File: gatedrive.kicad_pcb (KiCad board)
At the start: 2 copper layers, 200.7 x 101.6 mm, 159 parts, among them IC1 HCPL-316J, IC10 IXDD614PI, IC11 HCPL-316J, IC12 IXDD614PI, IC13 HCPL-316J, IC14 IXDD614PI, IC15 HCPL-316J, IC16 IXDD614PI, IC2 IXDD614PI, IC3 HCPL-316J, IC4 IXDD614PI, IC5 HCPL-316J, IC6 IXDD614PI, IC7 HCPL-316J, IC8 IXDD614PI, IC9 HCPL-316J, P1 Mic General Connector, P10 CONN_01X03, P11 CONN_01X03, P12 CONN_01X03, P13 CONN_01X03, P14 CONN_01X03, P15 CONN_01X03, P16 CONN_01X03, P17 CONN_01X03, P2 CONN_01X03, P3 CONN_01X03, P4 CONN_01X03, P5 CONN_01X03, P6 CONN_01X03, P7 CONN_01X03, P8 CONN_01X03, P9 CONN_01X03

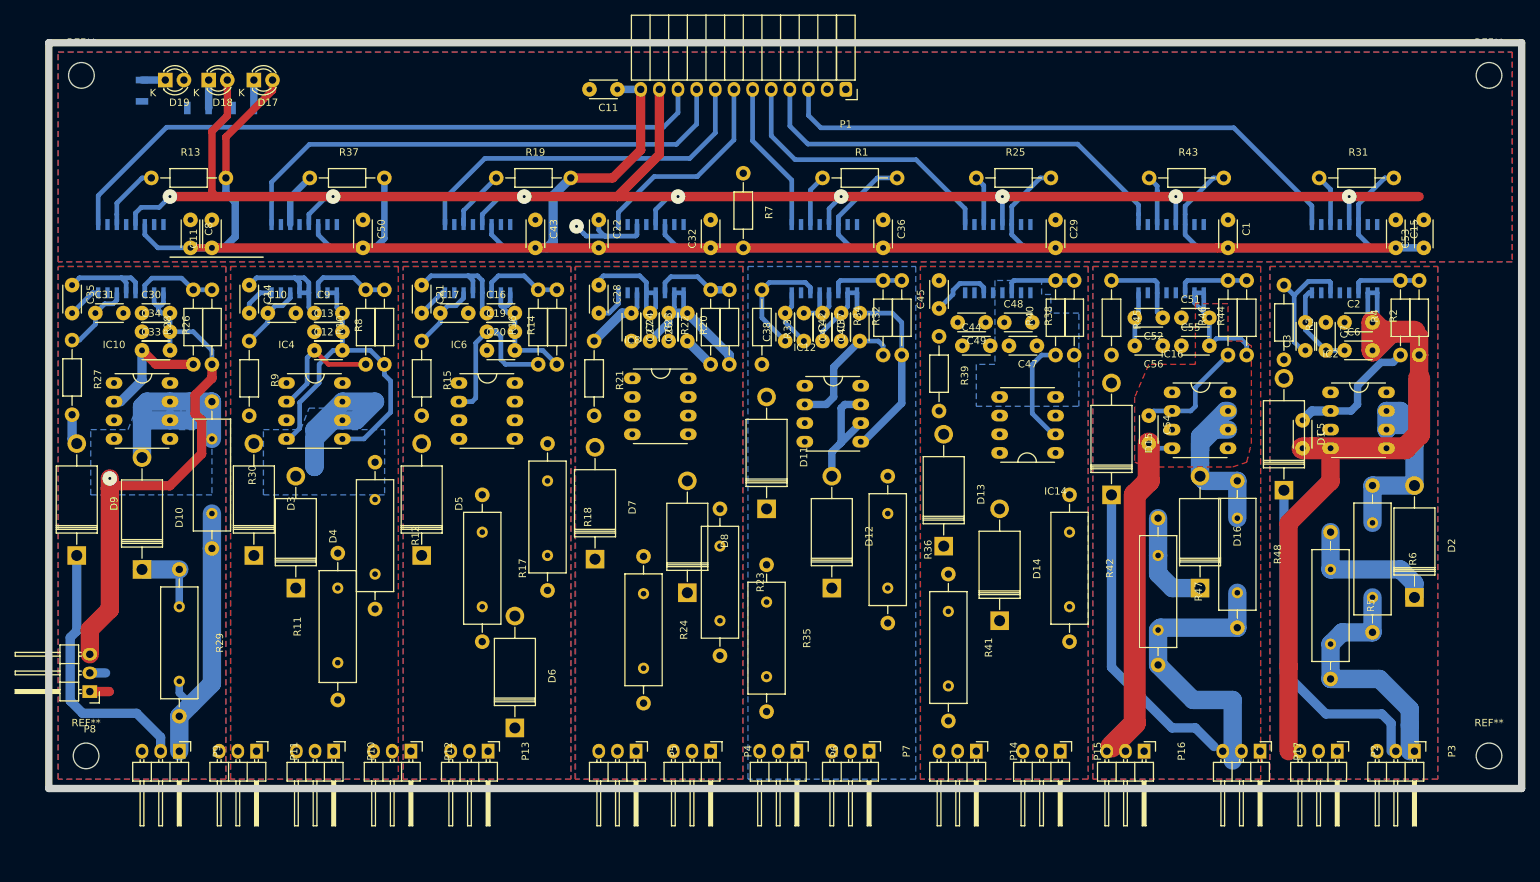
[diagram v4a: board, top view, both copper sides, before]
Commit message: cleaning the schematic
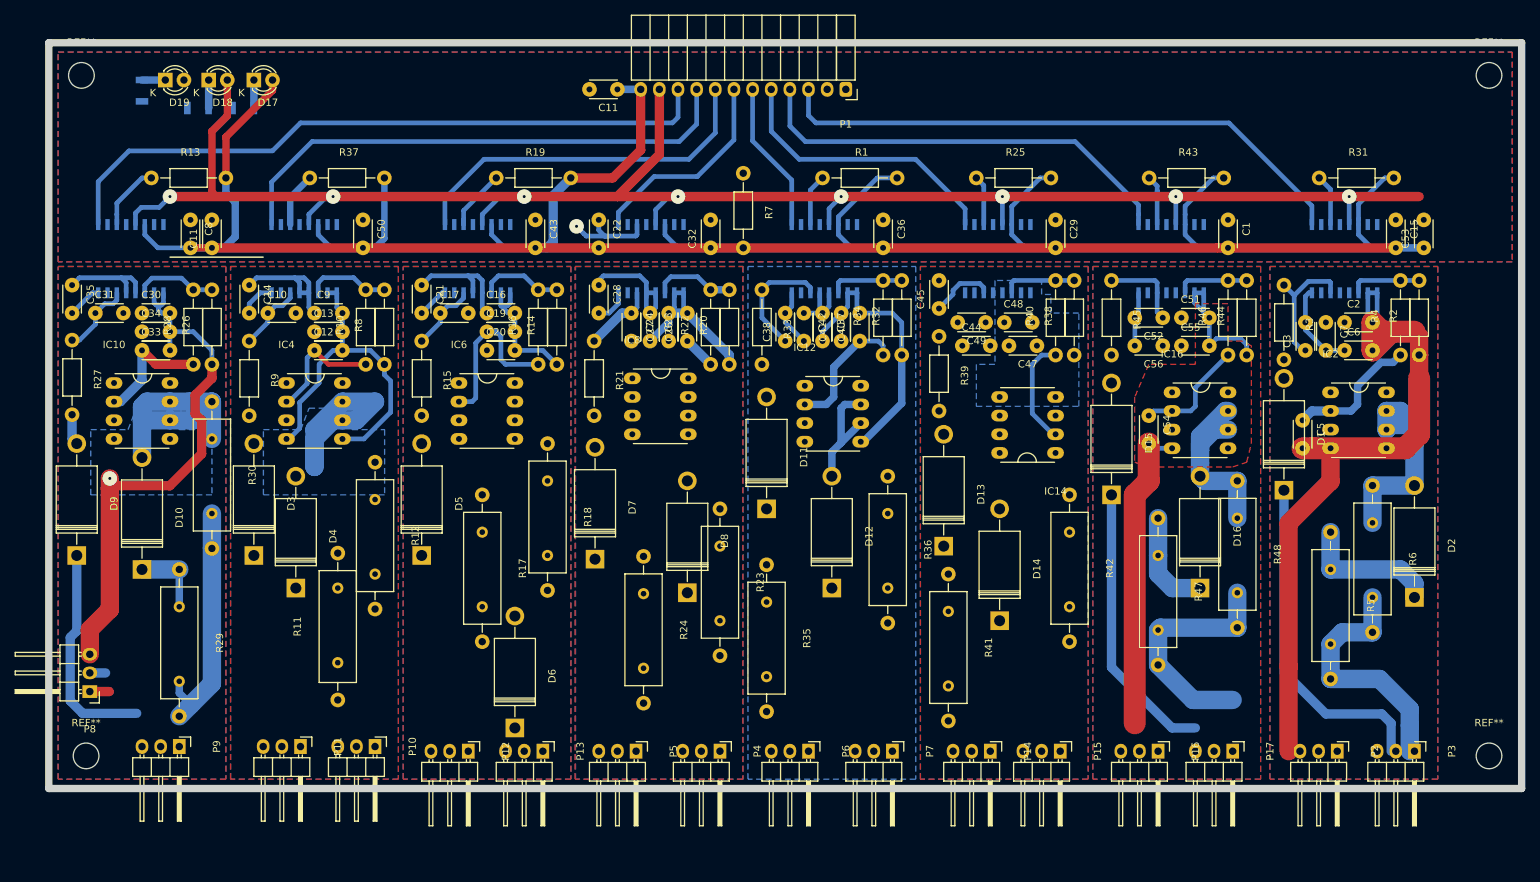
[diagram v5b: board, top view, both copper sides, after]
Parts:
- moved P12 7.82 mm to (96.2, 134.7)
- moved P13 7.46 mm to (106.3, 134.7)
- moved P11 6.03 mm to (73.3, 134.1)
- moved P10 5.67 mm to (83.5, 134.1)
- moved P17 3.73 mm to (200.3, 134.7)
- moved P7 3.17 mm to (154.0, 134.7)
- moved P14 1.91 mm to (167.3, 134.7)
- moved P16 1.91 mm to (190.2, 134.7)
- moved P6 1.59 mm to (142.5, 134.7)
- moved P4 1.27 mm to (130.5, 134.7)
- moved P9 0.63 mm to (56.8, 134.1)
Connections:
- net T1 renamed /T1
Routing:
- net G2: track 40.8 -> 32.6 mm
- net c8: track 36.5 -> 29.9 mm
- net G8: track 38.1 -> 33.3 mm
- net -5V2: track 67.1 -> 62.6 mm
- net C2: track 41.9 -> 38.3 mm
- net /T8: track 90.8 -> 92.3 mm

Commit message: completion of the layout, initial layout of the protection circuit, reducing number of circuit to 7
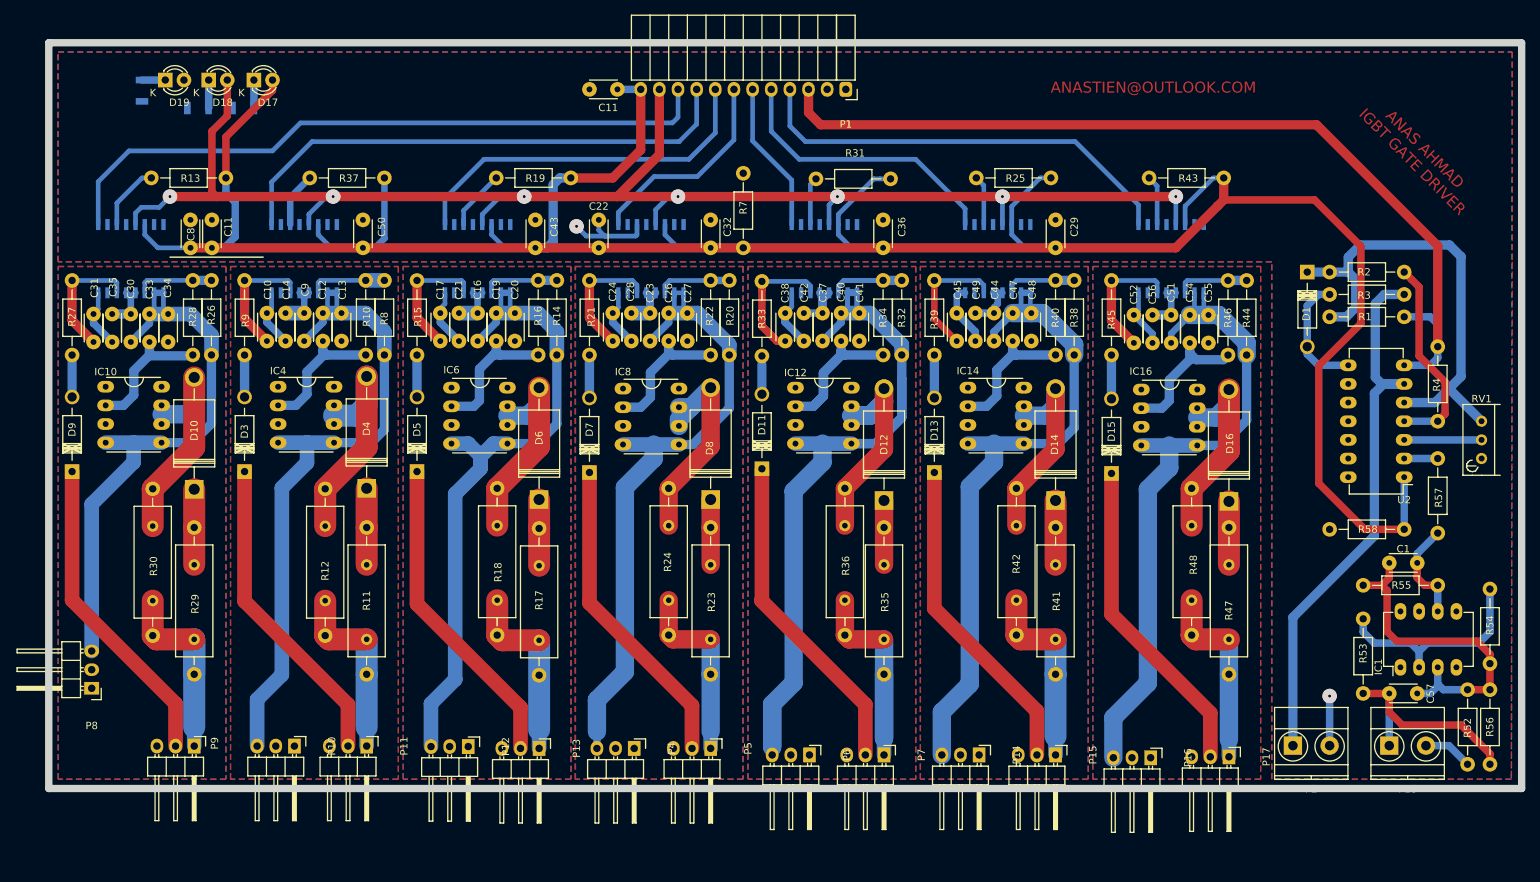
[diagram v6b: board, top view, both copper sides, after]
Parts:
- removed C15, C2, C6, C7: 0.1uF, gatedrive:C_Disc
- removed C3: 100pF, gatedrive:C_Disc
- removed C5: 10nF, gatedrive:C_Disc
- removed C53: 330pF, gatedrive:C_Disc
- removed D2: ~, Diodes_ThroughHole:Diode_DO-201AD_Horizontal_RM15
- removed IC2: IXDD614PI, gatedrive:DIP-8_W7.62mm_LongPads
- removed P3: CONN_01X03, Pin_Headers:Pin_Header_Angled_1x03
- removed R5: 60, gatedrive:Resistor_multi
- removed R6: 30ohm ,0.5W, gatedrive:Resistor_multi
- removed REF** (x4): MountingHole_3-5mm, Mounting_Holes:MountingHole_3-5mm
- added C57: 330p, gatedrive:C_Disc, F.Cu at (225.5, 126.8)
- added P18: FromShuntResistor, Terminal_Blocks:TerminalBlock_Pheonix_MKDS1.5-2pol, F.Cu at (221.7, 133.9)
- added R52: 1.24k, Resistors_ThroughHole:Resistor_Horizontal_RM10mm, F.Cu at (232.3, 126.3)
- added R53: 1.24k, Resistors_ThroughHole:Resistor_Horizontal_RM10mm, F.Cu at (218.1, 126.8)
- added R54: 20k, Resistors_ThroughHole:Resistor_Horizontal_RM10mm, F.Cu at (235.4, 112.6)
- added R55: 1.24k, Resistors_ThroughHole:Resistor_Horizontal_RM10mm, F.Cu at (218.1, 112.1)
- added R56: 1.24k, Resistors_ThroughHole:Resistor_Horizontal_RM10mm, F.Cu at (235.4, 126.3)
- added R57: 1.24k, Resistors_ThroughHole:Resistor_Horizontal_RM10mm, F.Cu at (228.3, 105.0)
- added R58: 1.24k, Resistors_ThroughHole:Resistor_Horizontal_RM10mm, F.Cu at (213.5, 104.5)
- added RV1: POT, Potentiometers:Potentiometer_Bourns_3296W_3-8Zoll_Inline_ScrewUp, F.Cu at (234.2, 94.8)
- added U2: LM393, Housings_DIP:DIP-14_W7.62mm_LongPads, F.Cu at (223.7, 97.4)
- C1: value 0.1uF -> 330p
- D1: value RGPO2-20 -> ZENER; footprint Diodes_ThroughHole:Diode_DO-201AD_Horizontal_RM15 -> Diodes_ThroughHole:Diode_DO-41_SOD81_Horizontal_RM10
- D11, D13, D15, D3, D5, D7, D9: footprint Diodes_ThroughHole:Diode_DO-201AD_Horizontal_RM15 -> Diodes_ThroughHole:Diode_DO-41_SOD81_Horizontal_RM10
- IC1: value HCPL-316J -> uA741_RevA_14Sep2012; footprint Housings_SOIC:SOIC-16_7.5x10.3mm_Pitch1.27mm -> Housings_DIP:DIP-8_W7.62mm_LongPads; moved to F.Cu
- P2: value CONN_01X03 -> FromNtc; footprint Pin_Headers:Pin_Header_Angled_1x03 -> Terminal_Blocks:TerminalBlock_Pheonix_MKDS1.5-2pol
- R1: value 10K -> 2.2MEG
- R2: value 25K -> 560
- R3: value 100 -> 10K
- R4: value 100 -> 1.24k
- moved R1 71.6 mm to (213.5, 75.5)
- moved R31 68.6 mm to (143.5, 56.7)
- moved IC1 56.2 mm to (223.2, 123.3), turned to 90 degrees
- moved C1 53.4 mm to (225.5, 109.1), turned to 180 degrees
- moved D6 31.3 mm to (105.8, 100.4)
- moved D1 29.9 mm to (210.5, 69.4), turned to 270 degrees
- moved R11 23.8 mm to (82.3, 104.2), turned to 270 degrees
- moved D14 18.1 mm to (176.2, 100.5)
- moved R35 16.8 mm to (152.8, 104.2)
- moved D4 16.7 mm to (82.3, 98.9)
- moved R3 16.4 mm to (223.7, 72.5), turned to 180 degrees
- moved R41 15.9 mm to (176.2, 104.2)
- moved IC14 14.9 mm to (164.2, 85.2), turned to 0 degrees
- moved R30 14.4 mm to (53.2, 99.0)
- moved D12 13.9 mm to (152.8, 100.5)
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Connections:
- C1 pad 1: MICSUPP -> Net-(C1-Pad1)
- C1 pad 2: ~FAULT -> Net-(C1-Pad2)
- D1 pad 1: C1 -> Net-(D1-Pad1)
- D1 pad 2: Net-(D1-Pad2) -> GND1
- IC1 pad 1: /T1 -> (no net)
- IC1 pad 2: GND1 -> Net-(IC1-Pad2)
- IC1 pad 3: MICSUPP -> Net-(C1-Pad2)
- IC1 pad 4: GND1 -> (no net)
- IC1 pad 5: ~RST -> (no net)
- IC1 pad 6: ~FAULT -> Net-(C1-Pad1)
- IC1 pad 7: Net-(IC1-Pad7) -> (no net)
- IC1 pad 8: GND1 -> (no net)
- IC11 pad 15: Net-(IC11-Pad15) -> (no net)
- IC11 pad 7: Net-(IC11-Pad7) -> (no net)
- IC13 pad 15: Net-(IC13-Pad15) -> (no net)
- IC13 pad 7: Net-(IC13-Pad7) -> (no net)
- IC15 pad 15: Net-(IC15-Pad15) -> (no net)
- IC15 pad 7: Net-(IC15-Pad7) -> (no net)
- IC3 pad 15: Net-(IC3-Pad15) -> (no net)
- IC3 pad 7: Net-(IC3-Pad7) -> (no net)
- IC5 pad 15: Net-(IC5-Pad15) -> (no net)
- IC5 pad 7: Net-(IC5-Pad7) -> (no net)
- IC7 pad 15: Net-(IC7-Pad15) -> (no net)
- IC7 pad 7: Net-(IC7-Pad7) -> (no net)
- IC9 pad 15: Net-(IC9-Pad15) -> (no net)
- IC9 pad 7: Net-(IC9-Pad7) -> (no net)
- P1 pad 3: /T1 -> ~OVERTEMP
- P11 pad 1: COM7 -> G7
- P11 pad 3: G7 -> COM7
- P13 pad 1: COM6 -> G6
- P13 pad 3: G6 -> COM6
- P2 pad 1: COM1 -> Net-(P2-Pad1)
- P2 pad 2: 15v1 -> MICSUPP
- R1 pad 1: MICSUPP -> Net-(D1-Pad1)
- R1 pad 2: ~FAULT -> ~OVERTEMP
- R2 pad 1: -5V1 -> MICSUPP
- R2 pad 2: Net-(IC1-Pad11) -> Net-(D1-Pad1)
- R3 pad 1: Net-(C3-Pad1) -> Net-(P2-Pad1)
- R3 pad 2: Net-(D1-Pad2) -> GND1
- R4 pad 1: Net-(C5-Pad1) -> MICSUPP
- R4 pad 2: Net-(IC1-Pad11) -> ~OVERTEMP
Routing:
- net ~OVERTEMP: track 0.00 -> 124.7 mm
- net -5V1: track 109.5 -> 0.00 mm
- net -5V3: track 0.00 -> 94.4 mm
- net -5V4: track 37.2 -> 123.9 mm
- net /T1: track 79.8 -> 0.00 mm
- net -5V6: track 18.5 -> 94.9 mm
- net Net-(P2-Pad1): track 0.00 -> 75.7 mm
- net -5V5: track 24.5 -> 92.5 mm
- net Net-(D1-Pad1): track 0.00 -> 65.6 mm
- net -5V7: track 47.1 -> 94.3 mm
- net C1: track 46.1 -> 0.00 mm
- net Net-(C1-Pad2): track 0.00 -> 45.9 mm
- net C4: track 0.00 -> 44.9 mm
- net C3: track 0.00 -> 44.3 mm
- net C6: track 0.00 -> 43.6 mm
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- added copper zone on F.Cu, net COM4
- removed copper zone on F.Cu, net -5V2
- removed copper zone on B.Cu, net -5V3
- removed copper zone on B.Cu, net -5V7
- removed copper zone on B.Cu, net -5v8
- removed copper zone on B.Cu, net 15v1
- removed copper zone on F.Cu, net COM1
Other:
- outline, holes or cut-outs redrawn
- board text added: "ANAS AHMAD IGBT GATE DRIVER"
- board text added: "ANASTIEN@OUTLOOK.COM"

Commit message: yet another enhancements .
the protection section still is incomplete.
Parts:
- added REF**: MountingHole_2.5mm, Mounting_Holes:MountingHole_2.5mm, F.Cu at (125.7, 134.0)
- added REF**: MountingHole_2.5mm, Mounting_Holes:MountingHole_2.5mm, F.Cu at (196.2, 134.0)
- added REF**: MountingHole_2.5mm, Mounting_Holes:MountingHole_2.5mm, F.Cu at (230.5, 47.6)
- added REF**: MountingHole_2.5mm, Mounting_Holes:MountingHole_2.5mm, F.Cu at (166.4, 48.9)
- added REF**: MountingHole_2.5mm, Mounting_Holes:MountingHole_2.5mm, F.Cu at (95.9, 48.9)
- added REF**: MountingHole_2.5mm, Mounting_Holes:MountingHole_2.5mm, F.Cu at (232.4, 134.0)
- added REF**: MountingHole_2.5mm, Mounting_Holes:MountingHole_2.5mm, F.Cu at (56.5, 134.0)
- moved R58 66.1 mm to (175.9, 50.2)
- moved U2 52.3 mm to (191.8, 55.9), turned to 90 degrees
- moved P2 51.7 mm to (223.5, 84.5), turned to 90 degrees
- moved R57 47.8 mm to (221.0, 57.8)
- moved RV1 35.5 mm to (226.1, 60.3), turned to 180 degrees
- moved R4 29.1 mm to (211.5, 66.0)
- moved D11 27.4 mm to (151.8, 118.7)
- moved D3 27.1 mm to (81.3, 118.7)
- moved D5 27.1 mm to (104.8, 118.7)
- moved D9 27.1 mm to (57.8, 118.7)
- moved D13 27.0 mm to (175.3, 118.7)
- moved D7 27.0 mm to (128.3, 118.7)
- moved D15 26.5 mm to (198.8, 118.7)
- moved R53 23.2 mm to (232.4, 108.6)
- moved C1 19.5 mm to (226.1, 89.5)
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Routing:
- net ~FAULT: track 380.7 -> 317.9 mm
- net Net-(C1-Pad1): track 14.0 -> 70.6 mm
- net ~OVERTEMP: track 124.7 -> 74.0 mm
- net MICSUPP: track 93.1 -> 53.7 mm, vias 2 -> 0
- net Net-(RV1-Pad2): track 10.5 -> 39.4 mm
- net Net-(R57-Pad2): track 4.57 -> 31.4 mm
- net Net-(P2-Pad1): track 75.7 -> 50.6 mm
- net Net-(D11-Pad2): track 4.06 -> 27.1 mm
- net -5V4: track 123.9 -> 101.6 mm
- net Net-(D5-Pad2): track 5.71 -> 27.8 mm
- net Net-(D7-Pad2): track 5.84 -> 27.8 mm
- net Net-(D3-Pad2): track 5.71 -> 27.5 mm
- net Net-(D9-Pad2): track 5.71 -> 27.5 mm
- net Net-(D13-Pad2): track 5.84 -> 27.5 mm
- net Net-(D15-Pad2): track 5.97 -> 27.5 mm
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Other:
- board outline removed
- board text removed: "ANAS AHMAD IGBT GATE DRIVER"
- board text removed: "ANASTIEN@OUTLOOK.COM"

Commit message: packup
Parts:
- removed the C1 at (226.1, 89.5)
- removed C10, C17, C24, C31, C38, C45, C52: 100pF, gatedrive:C_Disc
- removed C11 (x2), C32: 330pF, gatedrive:C_Disc
- removed C12, C19, C26, C33, C40, C47, C54: 10nF, gatedrive:C_Disc
- removed C13, C14, C16, C20, C21, C22, C23, C27, C28, C29, C30, C34, C35, C36, C37, C41, C42, C43, C44, C48, C49, C50, C51, C55, C56, C8, C9: 0.1uF, gatedrive:C_Disc
- removed C57: 330p, gatedrive:C_Disc
- removed D1: ZENER, Diodes_ThroughHole:Diode_DO-41_SOD81_Horizontal_RM10
- removed D10, D12, D14, D16, D4, D6, D8: ~, Diodes_ThroughHole:Diode_DO-201AD_Horizontal_RM15
- removed D11, D13, D15, D3, D5, D7, D9: RGPO2-20, Diodes_ThroughHole:Diode_DO-41_SOD81_Horizontal_RM10
- removed D17, D18, D19: LED, LEDs:LED-3MM
- removed IC1: uA741_RevA_14Sep2012, Housings_DIP:DIP-8_W7.62mm_LongPads
- removed IC10, IC12, IC14, IC16, IC4, IC6, IC8: IXDD614PI, gatedrive:DIP-8_W7.62mm_LongPads
- removed IC11, IC13, IC15, IC3, IC5, IC7, IC9: HCPL-316J, Housings_SOIC:SOIC-16_7.5x10.3mm_Pitch1.27mm
- removed P1: Mic General Connector, Socket_Strips:Socket_Strip_Angled_1x12
- removed P10, P11, P12, P13, P14, P15, P16, P17, P4, P5, P6, P7, P8, P9: CONN_01X03, Pin_Headers:Pin_Header_Angled_1x03
- removed P18: FromShuntResistor, Terminal_Blocks:TerminalBlock_Pheonix_MKDS1.5-2pol
- removed P2: FromNtc, Terminal_Blocks:TerminalBlock_Pheonix_MKDS1.5-2pol
- removed R1: 2.2MEG, Resistors_ThroughHole:Resistor_Horizontal_RM10mm
- removed R10, R15, R16, R21, R22, R27, R28, R33, R34, R39, R40, R45, R46, R9: 100, Resistors_ThroughHole:Resistor_Horizontal_RM10mm
- removed R11, R17, R23, R29, R35, R41, R47: 60, gatedrive:Resistor_multi
- removed R12, R18, R24, R30, R36, R42, R48: 30ohm ,0.5W, gatedrive:Resistor_multi
- removed R13, R19, R25, R3, R31, R37, R43, R7: 10K, Resistors_ThroughHole:Resistor_Horizontal_RM10mm
- removed R14, R20, R26, R32, R38, R44, R8: 25K, Resistors_ThroughHole:Resistor_Horizontal_RM10mm
- removed R2: 560, Resistors_ThroughHole:Resistor_Horizontal_RM10mm
- removed R4, R52, R53, R55, R56, R57, R58: 1.24k, Resistors_ThroughHole:Resistor_Horizontal_RM10mm
- removed R49, R50, R51: R, Resistors_SMD:R_1206
- removed R54: 20k, Resistors_ThroughHole:Resistor_Horizontal_RM10mm
- removed REF** (x7): MountingHole_2.5mm, Mounting_Holes:MountingHole_2.5mm
- removed RV1: POT, Potentiometers:Potentiometer_Bourns_3296W_3-8Zoll_Inline_ScrewUp
- removed U2: LM393, Housings_DIP:DIP-14_W7.62mm_LongPads
- added C1: 0.1u, gatedrive:C_Disc, F.Cu at (231.8, 99.7)
- added C1: 0.1u, gatedrive:C_Disc, F.Cu at (232.4, 64.8)
- added C201: 0.1uF, gatedrive:C_Disc, F.Cu at (201.3, 58.4)
- added C202: 330pF, gatedrive:C_Disc, F.Cu at (208.3, 70.5)
- added C203: 0.1uF, gatedrive:C_Disc, F.Cu at (205.1, 80.0)
- added C204: 0.1uF, gatedrive:C_Disc, F.Cu at (197.5, 83.8)
- added C205: 0.1uF, gatedrive:C_Disc, F.Cu at (200.0, 80.0)
- added C206: 100pF, gatedrive:C_Disc, F.Cu at (194.9, 83.8)
- added C207: 10nF, gatedrive:C_Disc, F.Cu at (202.6, 83.8)
- added C301: 0.1uF, gatedrive:C_Disc, F.Cu at (177.2, 57.8)
- added C302: 330pF, gatedrive:C_Disc, F.Cu at (184.8, 71.1)
- added C303: 0.1uF, gatedrive:C_Disc, F.Cu at (181.6, 80.0)
- added C304: 0.1uF, gatedrive:C_Disc, F.Cu at (174.0, 83.8)
- added C305: 0.1uF, gatedrive:C_Disc, F.Cu at (176.5, 80.0)
- added C306: 100pF, gatedrive:C_Disc, F.Cu at (171.4, 83.8)
- added C307: 10nF, gatedrive:C_Disc, F.Cu at (179.1, 83.8)
- added C401: 0.1uF, gatedrive:C_Disc, F.Cu at (154.9, 57.8)
- added C402: 330pF, gatedrive:C_Disc, F.Cu at (161.3, 71.1)
- added C403: 0.1uF, gatedrive:C_Disc, F.Cu at (158.1, 80.0)
- added C404: 0.1uF, gatedrive:C_Disc, F.Cu at (150.5, 83.8)
- added C405: 0.1uF, gatedrive:C_Disc, F.Cu at (153.0, 80.0)
- added C406: 100pF, gatedrive:C_Disc, F.Cu at (148.0, 83.8)
- added C407: 10nF, gatedrive:C_Disc, F.Cu at (155.6, 83.8)
- added C501: 0.1uF, gatedrive:C_Disc, F.Cu at (122.6, 67.3)
- added C502: 330pF, gatedrive:C_Disc, F.Cu at (137.8, 71.1)
- added C503: 0.1uF, gatedrive:C_Disc, F.Cu at (134.6, 80.0)
- added C504: 0.1uF, gatedrive:C_Disc, F.Cu at (127.0, 83.8)
- added C505: 0.1uF, gatedrive:C_Disc, F.Cu at (129.5, 80.0)
- added C506: 100pF, gatedrive:C_Disc, F.Cu at (124.5, 83.8)
- added C507: 10nF, gatedrive:C_Disc, F.Cu at (132.1, 83.8)
- added C601: 0.1uF, gatedrive:C_Disc, F.Cu at (111.1, 57.8)
- added C602: 330pF, gatedrive:C_Disc, F.Cu at (125.1, 49.5)
- added C602: 330pF, gatedrive:C_Disc, F.Cu at (116.2, 71.1)
- added C603: 0.1uF, gatedrive:C_Disc, F.Cu at (111.1, 80.0)
- added C604: 0.1uF, gatedrive:C_Disc, F.Cu at (103.5, 83.8)
- added C605: 0.1uF, gatedrive:C_Disc, F.Cu at (106.0, 80.0)
- added C606: 100pF, gatedrive:C_Disc, F.Cu at (101.0, 83.8)
- added C607: 10nF, gatedrive:C_Disc, F.Cu at (108.6, 83.8)
- added C701: 0.1uF, gatedrive:C_Disc, F.Cu at (86.4, 57.8)
- added C702: 330pF, gatedrive:C_Disc, F.Cu at (90.8, 71.1)
- added C703: 0.1uF, gatedrive:C_Disc, F.Cu at (87.6, 80.0)
- added C704: 0.1uF, gatedrive:C_Disc, F.Cu at (80.0, 83.8)
- added C705: 0.1uF, gatedrive:C_Disc, F.Cu at (82.5, 80.0)
- added C706: 100pF, gatedrive:C_Disc, F.Cu at (77.5, 83.8)
- added C707: 10nF, gatedrive:C_Disc, F.Cu at (85.1, 83.8)
- added C801: 33pf, gatedrive:C_Disc, F.Cu at (219.1, 123.8)
- added C802: 33p, gatedrive:C_Disc, F.Cu at (226.1, 106.0)
- added C901: 0.1uF, gatedrive:C_Disc, F.Cu at (64.8, 57.8)
- added C902: 330pF, gatedrive:C_Disc, F.Cu at (68.6, 71.1)
- added C903: 0.1uF, gatedrive:C_Disc, F.Cu at (64.1, 80.0)
- added C904: 0.1uF, gatedrive:C_Disc, F.Cu at (56.5, 83.8)
- added C905: 0.1uF, gatedrive:C_Disc, F.Cu at (59.1, 80.0)
- added C906: 100pF, gatedrive:C_Disc, F.Cu at (54.0, 83.8)
- added C907: 10nF, gatedrive:C_Disc, F.Cu at (61.6, 83.8)
- added D201: RGPO2-20, Diodes_ThroughHole:Diode_DO-41_SOD81_Horizontal_RM10, F.Cu at (198.8, 118.7)
- added D202: ~, Diodes_ThroughHole:Diode_DO-201AD_Horizontal_RM15, F.Cu at (207.6, 105.4)
- added D301: RGPO2-20, Diodes_ThroughHole:Diode_DO-41_SOD81_Horizontal_RM10, F.Cu at (175.3, 118.7)
- added D302: ~, Diodes_ThroughHole:Diode_DO-201AD_Horizontal_RM15, F.Cu at (184.2, 105.4)
- added D401: RGPO2-20, Diodes_ThroughHole:Diode_DO-41_SOD81_Horizontal_RM10, F.Cu at (151.8, 119.4)
- added D402: ~, Diodes_ThroughHole:Diode_DO-201AD_Horizontal_RM15, F.Cu at (160.7, 105.4)
- added D501: RGPO2-20, Diodes_ThroughHole:Diode_DO-41_SOD81_Horizontal_RM10, F.Cu at (128.3, 118.7)
- added D502: ~, Diodes_ThroughHole:Diode_DO-201AD_Horizontal_RM15, F.Cu at (137.2, 105.4)
- added D601: RGPO2-20, Diodes_ThroughHole:Diode_DO-41_SOD81_Horizontal_RM10, F.Cu at (104.8, 118.7)
- added D602: ~, Diodes_ThroughHole:Diode_DO-201AD_Horizontal_RM15, F.Cu at (113.7, 105.4)
- added D701: RGPO2-20, Diodes_ThroughHole:Diode_DO-41_SOD81_Horizontal_RM10, F.Cu at (81.3, 118.7)
- added D702: ~, Diodes_ThroughHole:Diode_DO-201AD_Horizontal_RM15, F.Cu at (90.2, 105.4)
- added D801: ZENER, Diodes_ThroughHole:Diode_DO-41_SOD81_Horizontal_RM10, F.Cu at (217.2, 88.3)
- added D901: RGPO2-20, Diodes_ThroughHole:Diode_DO-41_SOD81_Horizontal_RM10, F.Cu at (57.8, 118.7)
- added D902: ~, Diodes_ThroughHole:Diode_DO-201AD_Horizontal_RM15, F.Cu at (66.7, 105.4)
- added IC201: HCPL-316J, Housings_SOIC:SOIC-16_7.5x10.3mm_Pitch1.27mm, B.Cu at (200.0, 72.4)
- added IC202: IXDD614PI, gatedrive:DIP-8_W7.62mm_LongPads, F.Cu at (195.6, 90.2)
- added IC301: HCPL-316J, Housings_SOIC:SOIC-16_7.5x10.3mm_Pitch1.27mm, B.Cu at (176.5, 72.4)
- added IC302: IXDD614PI, gatedrive:DIP-8_W7.62mm_LongPads, F.Cu at (172.1, 90.2)
- added IC401: HCPL-316J, Housings_SOIC:SOIC-16_7.5x10.3mm_Pitch1.27mm, B.Cu at (153.0, 72.4)
- added IC402: IXDD614PI, gatedrive:DIP-8_W7.62mm_LongPads, F.Cu at (148.6, 90.2)
- added IC501: HCPL-316J, Housings_SOIC:SOIC-16_7.5x10.3mm_Pitch1.27mm, B.Cu at (129.5, 72.4)
- added IC502: IXDD614PI, gatedrive:DIP-8_W7.62mm_LongPads, F.Cu at (125.1, 90.2)
- added IC601: HCPL-316J, Housings_SOIC:SOIC-16_7.5x10.3mm_Pitch1.27mm, B.Cu at (106.0, 72.4)
- added IC602: IXDD614PI, gatedrive:DIP-8_W7.62mm_LongPads, F.Cu at (101.6, 90.2)
- added IC701: HCPL-316J, Housings_SOIC:SOIC-16_7.5x10.3mm_Pitch1.27mm, B.Cu at (82.5, 72.4)
- added IC702: IXDD614PI, gatedrive:DIP-8_W7.62mm_LongPads, F.Cu at (78.1, 90.2)
- added IC901: HCPL-316J, Housings_SOIC:SOIC-16_7.5x10.3mm_Pitch1.27mm, B.Cu at (59.1, 72.4)
- added IC902: IXDD614PI, gatedrive:DIP-8_W7.62mm_LongPads, F.Cu at (54.6, 90.2)
- added P101: Mic General Connector, Socket_Strips:Socket_Strip_Angled_1x12, F.Cu at (156.2, 49.5)
- added P201: CONN_01X03, gatedrive:conn, F.Cu at (194.3, 106.0)
- added P202: CONN_01X03, gatedrive:conn, F.Cu at (207.6, 137.8)
- added P301: CONN_01X03, gatedrive:conn, F.Cu at (170.8, 106.0)
- added P302: CONN_01X03, gatedrive:conn, F.Cu at (184.2, 137.8)
- added P401: CONN_01X03, gatedrive:conn, F.Cu at (147.3, 106.0)
- added P402: CONN_01X03, gatedrive:conn, F.Cu at (160.7, 137.8)
- added P501: CONN_01X03, gatedrive:conn, F.Cu at (123.8, 106.0)
- added P502: CONN_01X03, gatedrive:conn, F.Cu at (137.2, 137.8)
- added P601: CONN_01X03, gatedrive:conn, F.Cu at (100.3, 106.0)
- added P602: CONN_01X03, gatedrive:conn, F.Cu at (113.7, 137.8)
- added P701: CONN_01X03, gatedrive:conn, F.Cu at (76.8, 106.0)
- added P702: CONN_01X03, gatedrive:conn, F.Cu at (90.2, 137.8)
- added P801: FromShuntResistor, Terminal_Blocks:TerminalBlock_Pheonix_MKDS1.5-2pol, F.Cu at (220.4, 137.2)
- added P802: FromNtc, Terminal_Blocks:TerminalBlock_Pheonix_MKDS1.5-2pol, F.Cu at (221.6, 119.4)
- added P901: CONN_01X03, gatedrive:conn, F.Cu at (53.3, 106.0)
- added P902: CONN_01X03, gatedrive:conn, F.Cu at (66.7, 137.8)
- added R201: 10K, Resistors_ThroughHole:Resistor_Horizontal_RM10mm, F.Cu at (208.3, 61.6)
- added R202: 25K, Resistors_ThroughHole:Resistor_Horizontal_RM10mm, F.Cu at (210.2, 86.4)
- added R203: 100, Resistors_ThroughHole:Resistor_Horizontal_RM10mm, F.Cu at (192.4, 76.2)
- added R204: 100, Resistors_ThroughHole:Resistor_Horizontal_RM10mm, F.Cu at (207.6, 86.4)
- added R205: 60, gatedrive:Resistor_multi, F.Cu at (207.6, 111.8)
- added R206: 30ohm ,0.5W, gatedrive:Resistor_multi, F.Cu at (202.6, 107.0)
- added R301: 10K, Resistors_ThroughHole:Resistor_Horizontal_RM10mm, F.Cu at (184.2, 61.0)
- added R302: 25K, Resistors_ThroughHole:Resistor_Horizontal_RM10mm, F.Cu at (186.7, 86.4)
- added R303: 100, Resistors_ThroughHole:Resistor_Horizontal_RM10mm, F.Cu at (168.9, 76.2)
- added R304: 100, Resistors_ThroughHole:Resistor_Horizontal_RM10mm, F.Cu at (184.2, 86.4)
- added R305: 60, gatedrive:Resistor_multi, F.Cu at (184.2, 111.8)
- added R306: 30ohm ,0.5W, gatedrive:Resistor_multi, F.Cu at (179.1, 107.0)
- added R401: 10K, Resistors_ThroughHole:Resistor_Horizontal_RM10mm, F.Cu at (161.9, 61.0)
- added R402: 25K, Resistors_ThroughHole:Resistor_Horizontal_RM10mm, F.Cu at (163.2, 86.4)
- added R403: 100, Resistors_ThroughHole:Resistor_Horizontal_RM10mm, F.Cu at (145.4, 76.2)
- added R404: 100, Resistors_ThroughHole:Resistor_Horizontal_RM10mm, F.Cu at (160.7, 86.4)
- added R405: 60, gatedrive:Resistor_multi, F.Cu at (160.7, 111.8)
- added R406: 30ohm ,0.5W, gatedrive:Resistor_multi, F.Cu at (155.6, 107.0)
- added R501: 10K, Resistors_ThroughHole:Resistor_Horizontal_RM10mm, F.Cu at (142.2, 71.1)
- added R502: 25K, Resistors_ThroughHole:Resistor_Horizontal_RM10mm, F.Cu at (139.7, 86.4)
- added R503: 100, Resistors_ThroughHole:Resistor_Horizontal_RM10mm, F.Cu at (121.9, 76.2)
- added R504: 100, Resistors_ThroughHole:Resistor_Horizontal_RM10mm, F.Cu at (137.2, 86.4)
- added R505: 60, gatedrive:Resistor_multi, F.Cu at (137.2, 111.8)
- added R506: 30ohm ,0.5W, gatedrive:Resistor_multi, F.Cu at (132.1, 107.0)
- added R601: 10K, Resistors_ThroughHole:Resistor_Horizontal_RM10mm, F.Cu at (118.1, 61.0)
- added R602: 25K, Resistors_ThroughHole:Resistor_Horizontal_RM10mm, F.Cu at (116.2, 86.4)
- added R603: 100, Resistors_ThroughHole:Resistor_Horizontal_RM10mm, F.Cu at (98.4, 76.2)
- added R604: 100, Resistors_ThroughHole:Resistor_Horizontal_RM10mm, F.Cu at (113.7, 86.4)
- added R605: 60, gatedrive:Resistor_multi, F.Cu at (113.7, 111.8)
- added R606: 30ohm ,0.5W, gatedrive:Resistor_multi, F.Cu at (108.6, 107.0)
- added R701: 10K, Resistors_ThroughHole:Resistor_Horizontal_RM10mm, F.Cu at (93.3, 61.0)
- added R702: 25K, Resistors_ThroughHole:Resistor_Horizontal_RM10mm, F.Cu at (92.7, 86.4)
- added R703: 100, Resistors_ThroughHole:Resistor_Horizontal_RM10mm, F.Cu at (74.9, 76.2)
- added R704: 100, Resistors_ThroughHole:Resistor_Horizontal_RM10mm, F.Cu at (90.2, 86.4)
- added R705: 60, gatedrive:Resistor_multi, F.Cu at (90.2, 111.8)
- added R706: 30ohm ,0.5W, gatedrive:Resistor_multi, F.Cu at (85.1, 107.0)
- added R801: 1.24k, Resistors_ThroughHole:Resistor_Horizontal_RM10mm, F.Cu at (215.9, 140.3)
- added R802: 1.24k, Resistors_ThroughHole:Resistor_Horizontal_RM10mm, F.Cu at (229.9, 134.0)
- added R803: 20k, Resistors_ThroughHole:Resistor_Horizontal_RM10mm, F.Cu at (233.0, 134.0)
- added R804: 61.9k, Resistors_ThroughHole:Resistor_Horizontal_RM10mm, F.Cu at (226.1, 126.4)
- added R805: 61.9k, Resistors_ThroughHole:Resistor_Horizontal_RM10mm, F.Cu at (229.2, 108.6)
- added R806: 560, Resistors_ThroughHole:Resistor_Horizontal_RM10mm, F.Cu at (224.8, 89.5)
- added R807: 10K, Resistors_ThroughHole:Resistor_Horizontal_RM10mm, F.Cu at (221.0, 89.5)
- added R808: 10k, Resistors_ThroughHole:Resistor_Horizontal_RM10mm, F.Cu at (228.6, 89.5)
- added R809: 2.2MEG, Resistors_ThroughHole:Resistor_Horizontal_RM10mm, F.Cu at (217.2, 74.9)
- added R810: 10k, Resistors_ThroughHole:Resistor_Horizontal_RM10mm, F.Cu at (219.1, 55.9)
- added R811: 1.24k, Resistors_ThroughHole:Resistor_Horizontal_RM10mm, F.Cu at (229.2, 52.7)
- added R901: 10K, Resistors_ThroughHole:Resistor_Horizontal_RM10mm, F.Cu at (71.8, 61.0)
- added R902: 25K, Resistors_ThroughHole:Resistor_Horizontal_RM10mm, F.Cu at (69.2, 86.4)
- added R903: 100, Resistors_ThroughHole:Resistor_Horizontal_RM10mm, F.Cu at (51.4, 76.2)
- added R904: 100, Resistors_ThroughHole:Resistor_Horizontal_RM10mm, F.Cu at (66.7, 86.4)
- added R905: 60, gatedrive:Resistor_multi, F.Cu at (66.7, 111.8)
- added R906: 30ohm ,0.5W, gatedrive:Resistor_multi, F.Cu at (61.6, 107.0)
- added RV801: 10k, Potentiometers:Potentiometer_Bourns_3296W_3-8Zoll_Inline_ScrewUp, F.Cu at (212.7, 65.4)
- added U802: LM339, Housings_DIP:DIP-14_W7.62mm_LongPads, F.Cu at (221.0, 59.7)
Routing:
- net -5V5: track 106.9 -> 0.00 mm
- net -5V4: track 101.6 -> 0.00 mm
- net +5V: track 0.00 -> 96.4 mm
- net -5V7: track 95.6 -> 0.00 mm
- net -5V6: track 95.2 -> 0.00 mm
- net -5V3: track 94.3 -> 0.00 mm
- net -5V2: track 94.2 -> 0.00 mm
- net -5v8: track 93.2 -> 0.00 mm
- net /T8: track 91.2 -> 0.00 mm
- net /T1: track 0.00 -> 90.3 mm
- net Net-(C1-Pad1): track 70.6 -> 0.00 mm
- net Net-(C1-Pad2): track 66.9 -> 0.00 mm
- net MICSUPP: track 53.7 -> 0.00 mm
- net -5v3: track 0.00 -> 53.6 mm
- net -5v2: track 0.00 -> 53.6 mm
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- added copper zone on F.Cu, net +5V
- added copper zone on B.Cu, net 15V1
- added copper zone on F.Cu, net COM1
- added copper zone on B.Cu, net GND
- removed copper zone on B.Cu, net 15V8
- removed copper zone on F.Cu, net COM8
- removed copper zone on B.Cu, net GND1
- removed copper zone on F.Cu, net MICSUPP
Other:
- board outline added: 189.9 x 101 mm
- board text added: "1"
- board text added: "2"
- board text added: "3"
- board text added: "4"
- board text added: "5"
- board text added: "6"
- board text added: "7"
- board text added: "LENGTH = 20 cm"
- board text added: "T1 >"
- board text added: "VFD 7 IGBT GATE DRIVERS"
- board text added: "VFD IGBT gate driver BY ANAS AHMAD"
- board text added: "anastien@outlook.com"
